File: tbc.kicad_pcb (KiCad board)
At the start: 4 copper layers, 180 x 67 mm, 129 parts, among them J1 5749181-1, J2 PJRAN1X1U01X, J3 PJRAN1X1U01X, J4 5749181-1, J5 PJRAN1X1U01X, J6 PJRAN3X1U03X, J7 4840.2201, J8 20021111-00010T4LF, J9 75869-105LF, Q1 BSS308PE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

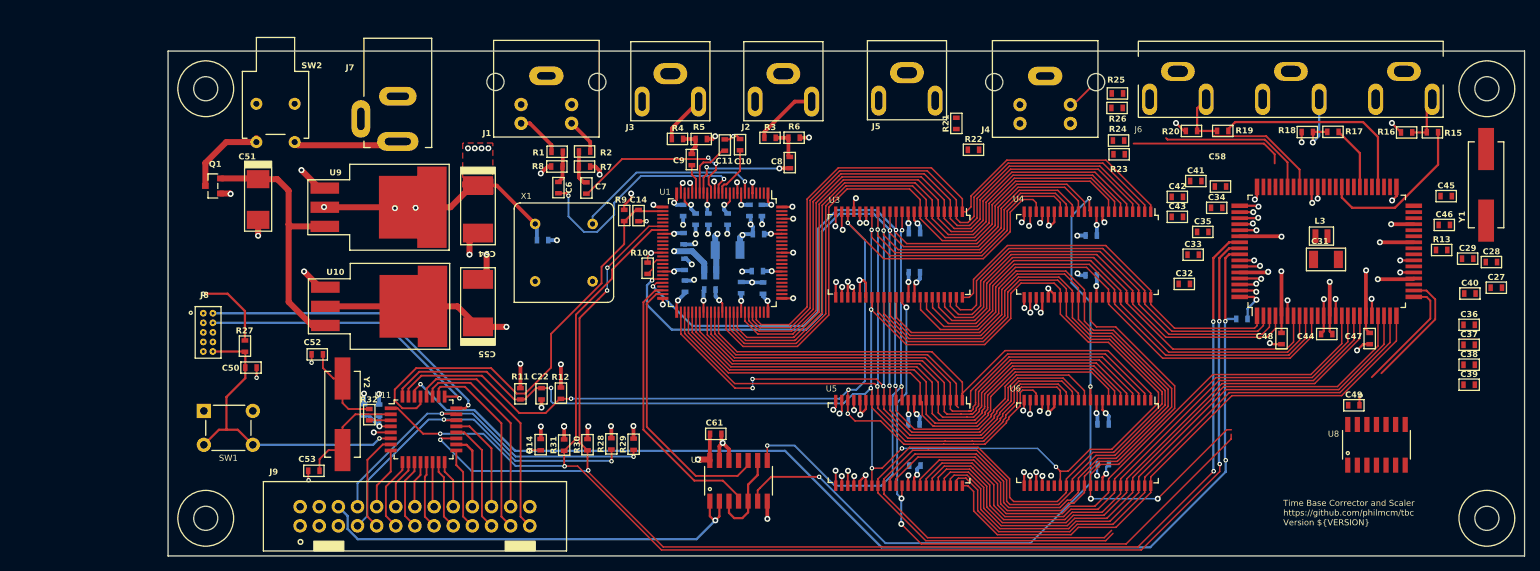
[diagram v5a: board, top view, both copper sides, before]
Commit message: layout complete and passed DRC
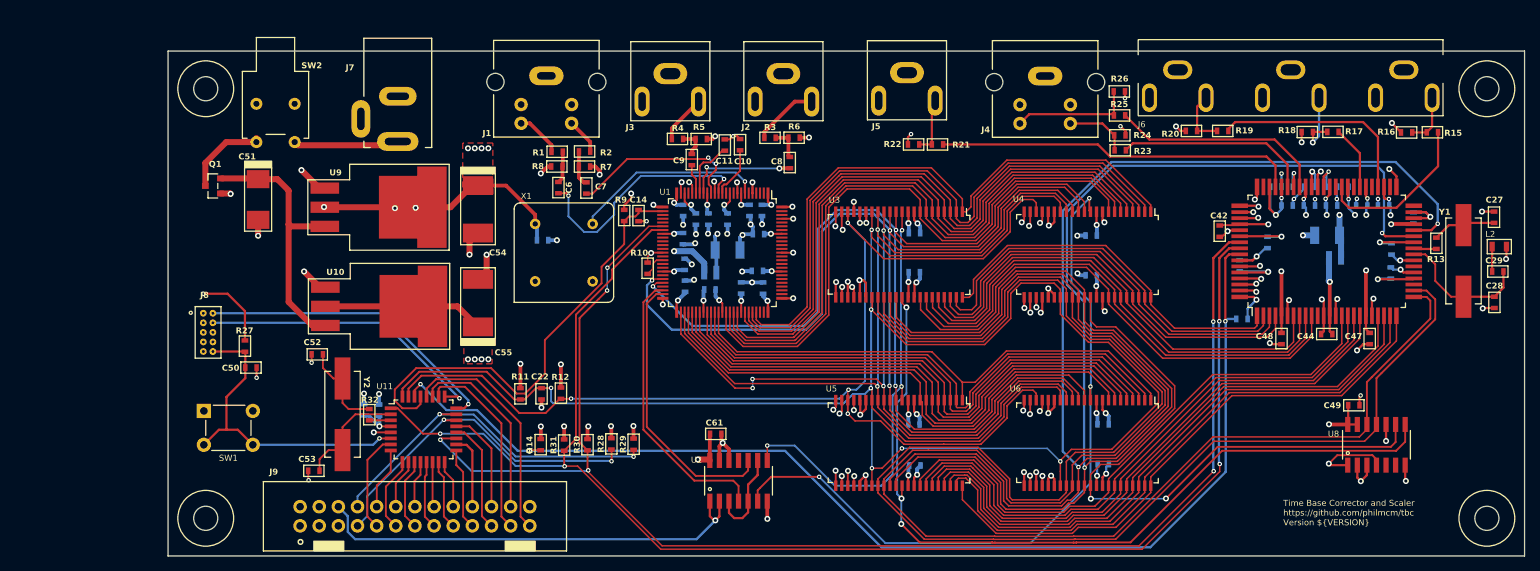
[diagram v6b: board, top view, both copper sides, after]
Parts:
- added L2: 10uH, tbc:L0805, F.Cu at (256.6, 91.0)
- C31, C32, C33, C34, C35, C36, C37, C38, C39, C40, C41, C43, C45, C46, C58, L3: moved to B.Cu
- moved C43 29.3 mm to (242.2, 94.5), turned to 90 degrees
- moved C38 29.0 mm to (235.9, 83.0), turned to 180 degrees
- moved C39 27.7 mm to (238.4, 85.5), turned to 180 degrees
- moved C36 26.9 mm to (232.9, 83.0), turned to 180 degrees
- moved C37 26.0 mm to (234.4, 85.5)
- moved C45 24.5 mm to (225.9, 90.4), turned to -90 degrees
- moved C58 24.2 mm to (242.3, 91.2), turned to 90 degrees
- moved C32 17.7 mm to (227.0, 83.0)
- moved C40 16.4 mm to (241.3, 85.5), turned to 180 degrees
- moved C35 14.6 mm to (231.4, 85.5)
- moved C33 14.1 mm to (228.5, 85.5)
- moved C41 12.7 mm to (222.2, 93.5), turned to 90 degrees
- moved C34 11.2 mm to (230.0, 83.0)
- moved Y1 10.5 mm to (251.9, 92.8)
- moved C27 9.35 mm to (255.9, 87.0), turned to 90 degrees
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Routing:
- net /Frame Memories and Freeze/LLC: track 106.5 -> 202.6 mm, vias 0 -> 2
- net /Frame Memories and Freeze/CREF: track 106.2 -> 199.1 mm, vias 0 -> 2
- net +3V3A2: track 0.00 -> 76.2 mm, vias 0 -> 15
- net /Frame Memories and Freeze/RCV2: track 158.9 -> 208.3 mm
- net +5V: track 354.4 -> 401.9 mm, vias 25 -> 31
- net /Frame Memories and Freeze/RCV1: track 157.1 -> 204.4 mm
- net GND: track 233.8 -> 277.8 mm, vias 110 -> 127
- net Net-(U7-CVBS): track 20.7 -> 48.1 mm
- net /Frame Memories and Freeze/Q2: track 83.8 -> 108.3 mm
- net /Frame Memories and Freeze/Q1: track 61.3 -> 84.8 mm
- net Net-(U7-XTALI): track 0.00 -> 18.2 mm
- net /Video Encoder/C_OUT: track 0.00 -> 16.2 mm
- net +3V3: track 357.6 -> 371.6 mm, vias 33 -> 32
- net Net-(U7-CHROMA): track 15.7 -> 28.9 mm
- net Net-(C27-Pad1): track 0.00 -> 8.46 mm
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- added copper zone on F.Cu, net +5V

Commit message: add PEC11R footprint, minor enhancements to layout
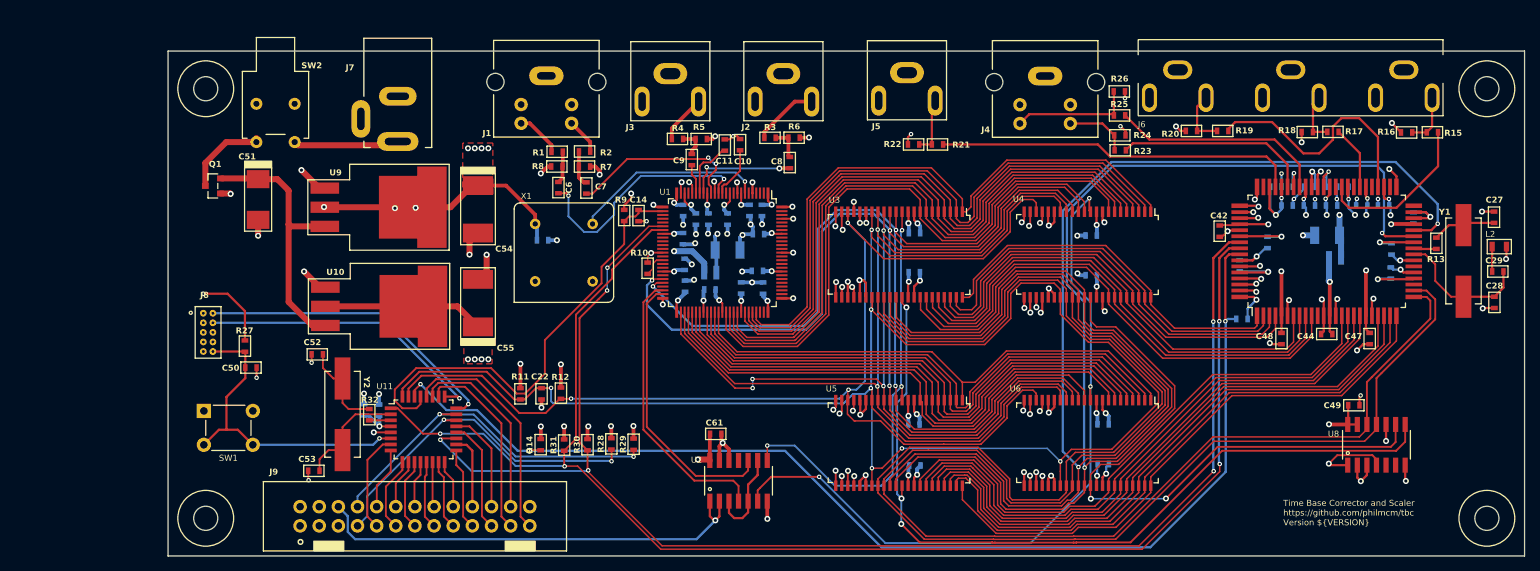
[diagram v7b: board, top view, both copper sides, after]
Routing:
- net Net-(U7-BLUE): track 27.9 -> 32.8 mm
- net /Video Encoder/G: track 10.7 -> 7.97 mm, vias 1 -> 0
- net +5V: track 401.9 -> 401.2 mm
- net /Frame Memories and Freeze/MEM_MODE: vias 4 -> 3

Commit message: update to Kicad 8.0, add gerbers
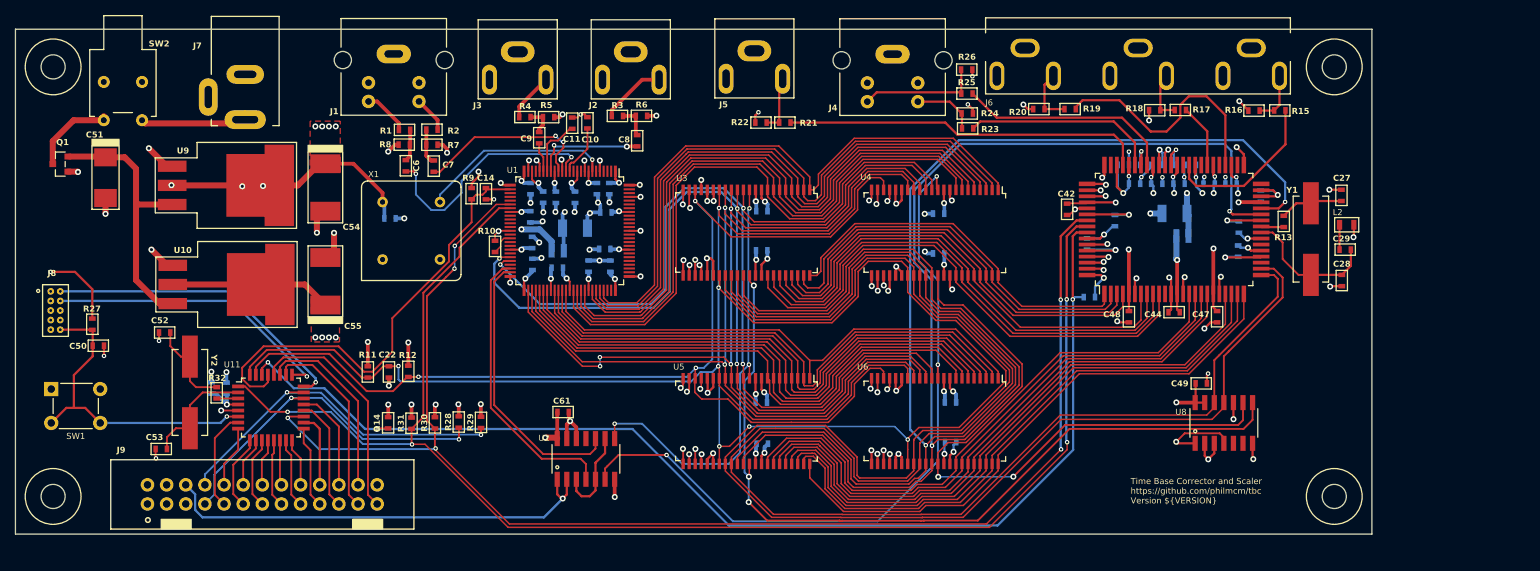
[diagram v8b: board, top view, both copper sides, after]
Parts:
- moved C6 20.5 mm to (111.5, 80.2)
- moved R2 20.5 mm to (115.0, 75.4)
- moved C1 20.5 mm to (134.0, 88.5)
- moved C10 20.5 mm to (135.7, 74.5)
- moved C11 20.5 mm to (133.6, 74.6)
- moved C12 20.5 mm to (137.9, 91.3)
- moved C13 20.5 mm to (138.1, 86.4)
- moved C14 20.5 mm to (122.2, 83.9)
- moved C15 20.5 mm to (138.7, 93.5)
- moved C16 20.5 mm to (138.6, 83.2)
- moved C17 20.5 mm to (128.1, 83.2)
- moved C18 20.5 mm to (128.3, 93.3)
- moved C19 20.5 mm to (128.3, 90.4)
- moved C2 20.5 mm to (129.8, 84.4)
- moved C20 20.5 mm to (131.7, 93.8)
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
